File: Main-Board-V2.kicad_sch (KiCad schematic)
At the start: 12 parts, among them IC1 REG1117-5, J4 1-776163-5, U1 OPA325IDBVR, U2 Teensy4.0

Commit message: added LED indicators, fixed footprints
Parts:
- added D2, D3: LED, LED_SMD:LED_0805_2012Metric, symbol Device:LED
- added R29, R32: R_US, Resistor_SMD:R_0805_2012Metric, symbol Device:R_US
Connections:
- net +12V: now also R32.1
- net +5V: now also R29.1
- net GND: now also D2.1 (K), D3.1 (K)
- new net: D2.2 (A), R29.2
- new net: D3.2 (A), R32.2
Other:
- note added: "LED Power Indicators"
- note added: "Teensy 4.0 Pinout"
- title: (none) -> Main Board 2024
- moved on the sheet: C1, C2, C3, IC1, J4, R1, R2, R3, R4, R5, U1, U2

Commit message: idk, probably nothing
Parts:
- R29, R32: value R_US -> 150R
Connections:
- no-connect marks 34 -> 32
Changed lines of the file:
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@@
 	)
 	(no_connect
-		(at 236.22 106.68)
-	)
-	(no_connect
 		(at 292.1 99.06)
 	)
@@
 	)
 	(no_connect
-		(at 236.22 109.22)
-	)
-	(no_connect
 		(at 66.04 55.88)
 	)
@@
 			)
 		)
-		(property "Value" "R_US"
+		(property "Value" "150R"
 			(at 205.74 208.2799 0)
 			(effects
@@
 			)
 		)
-		(property "Value" "R_US"
+		(property "Value" "150R"
 			(at 180.34 208.2799 0)
 			(effects

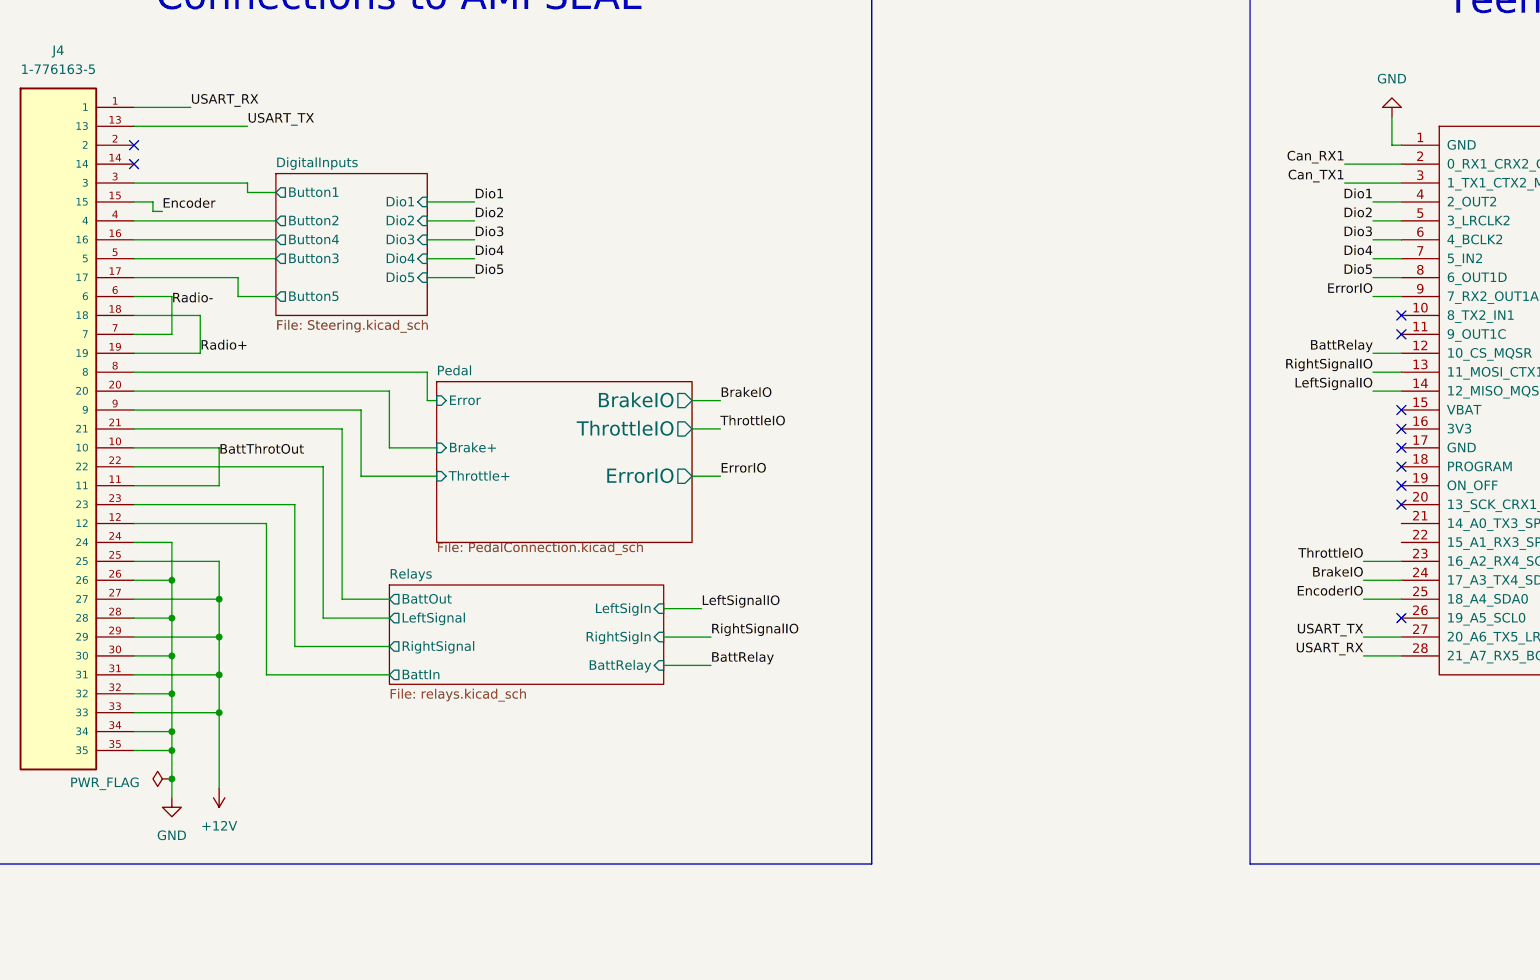
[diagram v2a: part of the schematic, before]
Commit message: redid 35 pos pinout
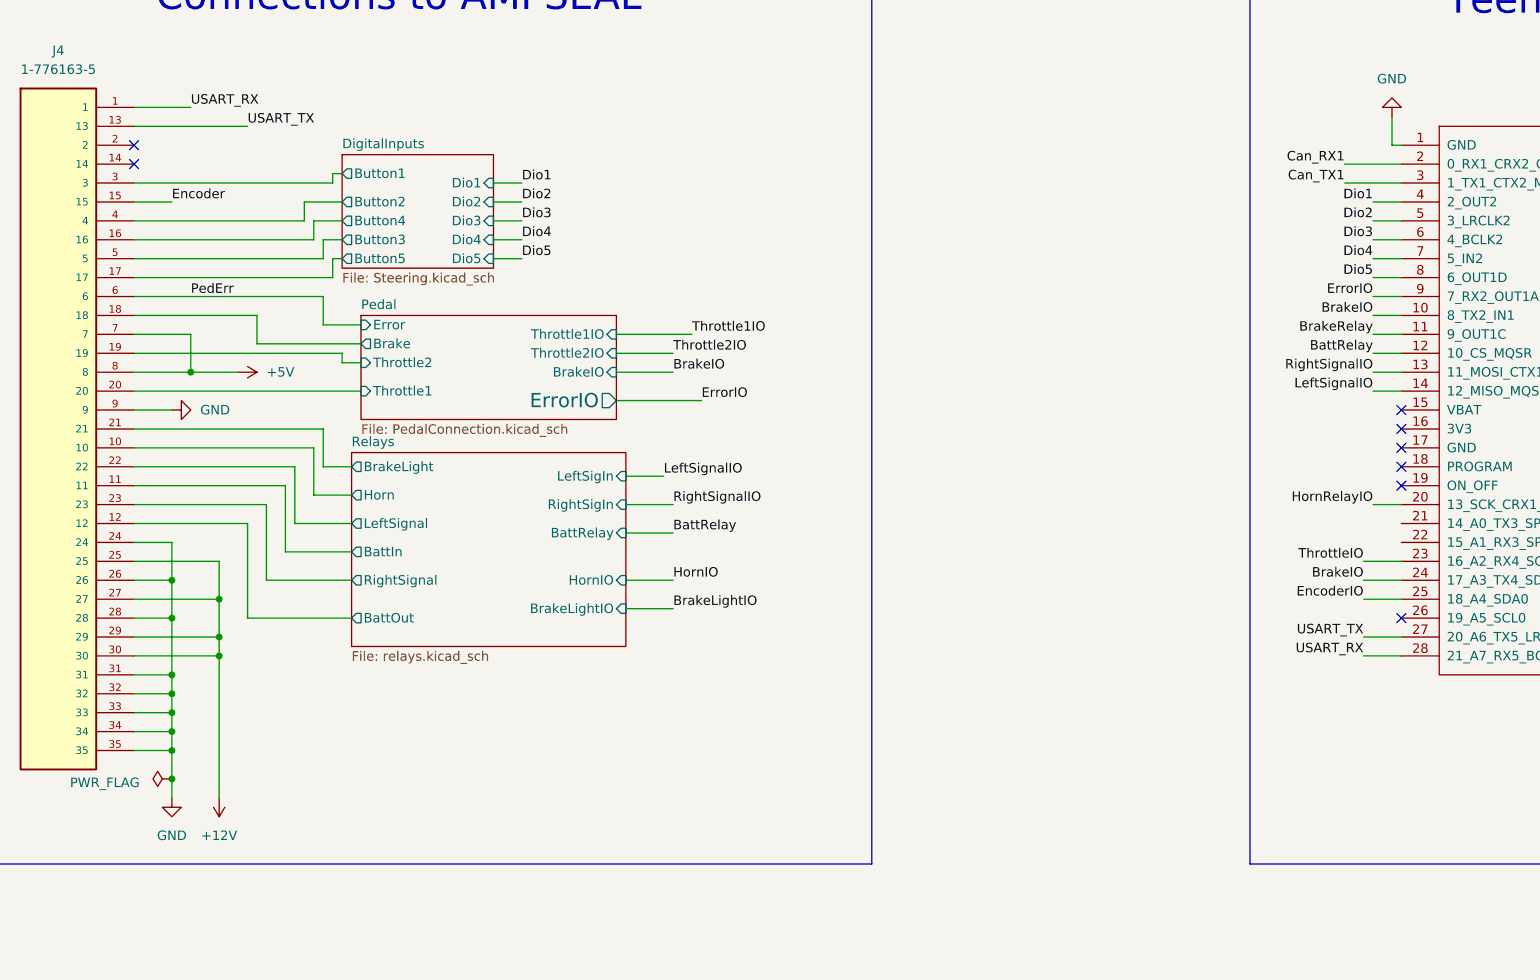
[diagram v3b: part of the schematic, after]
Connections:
- net Pedal/Error is gone; now on net +5V: J4.8
- net Pedal/Throttle+ is gone; now on net GND: J4.9
- net +12V: now also J4.30; no longer J4.31, J4.33
- net +5V: now also J4.7
- net BrakeIO: now also U2.10 (8_TX2_IN1)
- net GND: now also J4.31, J4.33; no longer J4.30
- net Relays/BattIn: now also J4.11; no longer J4.12
- net Relays/BattOut: now also J4.12; no longer J4.21
- net BrakeRelay: now reaches U2.11 (9_OUT1C)
- net HornRelayIO: now reaches U2.20 (13_SCK_CRX1_LED)
- net BattThrotOut renamed Relays/Horn
- net Relays/Horn: no longer J4.11
- net Pedal/Brake+ renamed Pedal/Throttle1
- net Radio+ renamed Pedal/Brake
- net Pedal/Brake: no longer J4.19
- net Radio- renamed PedErr
- net PedErr: no longer J4.7
- new net Pedal/Throttle2: J4.19
- new net Relays/BrakeLight: J4.21
- no-connect marks 32 -> 29
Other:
- sheet Pedal ports: added Brake, Throttle1, Throttle1IO, Throttle2, Throttle2IO; removed Brake+, Throttle+, ThrottleIO
- sheet Relays ports: added BrakeLight, BrakeLightIO, Horn, HornIO; removed none

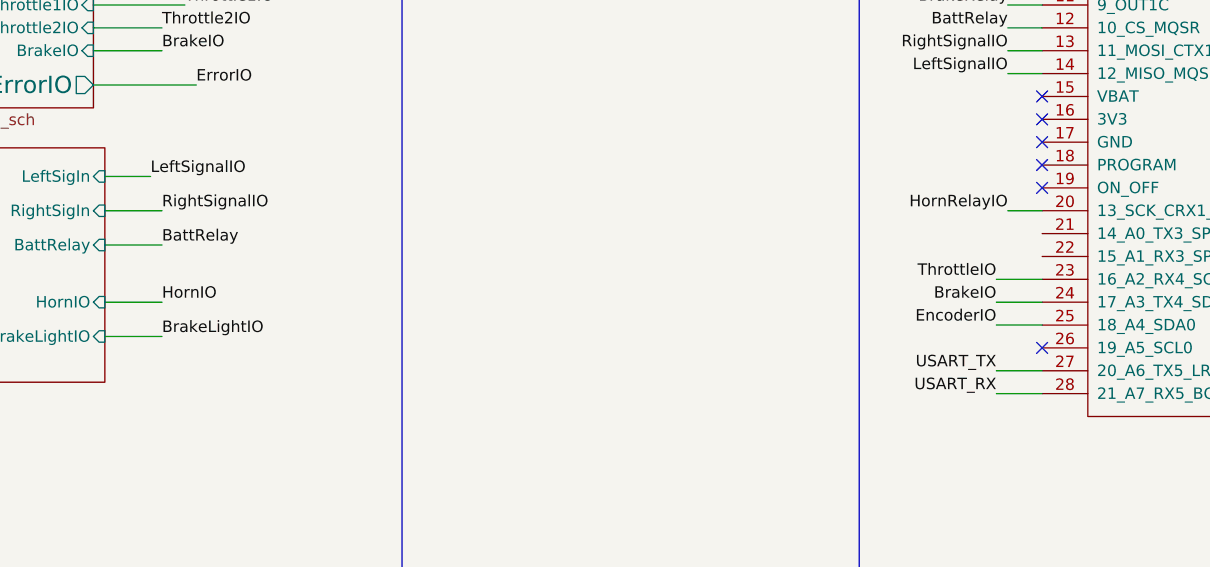
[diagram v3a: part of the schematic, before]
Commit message: fixed pcb excpet relays
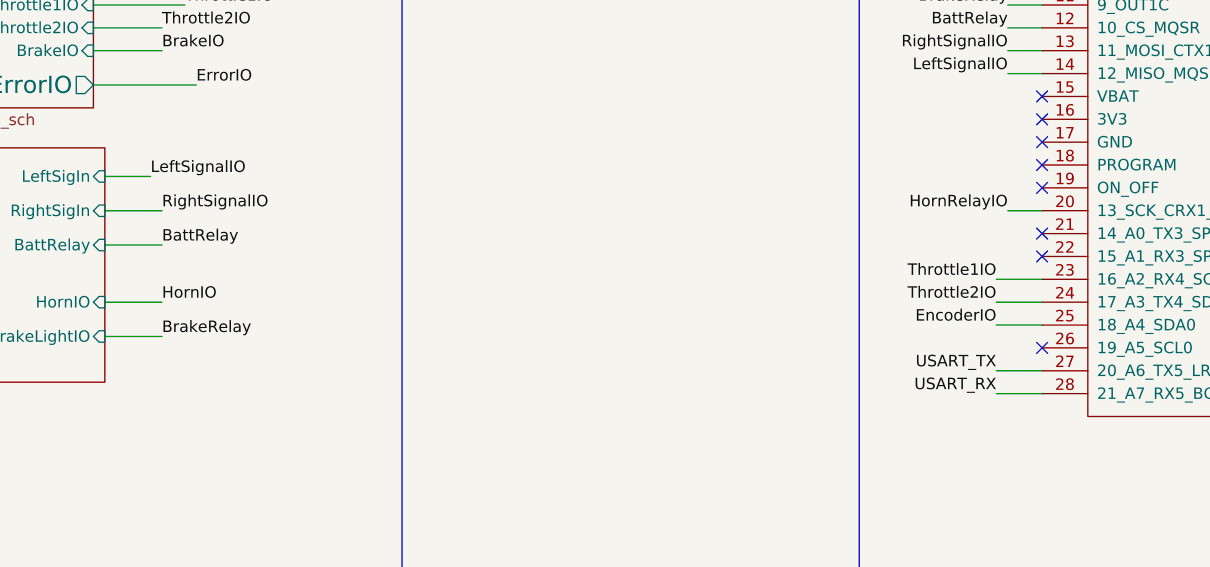
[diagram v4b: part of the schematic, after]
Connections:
- net ThrottleIO is gone; now on net Throttle1IO: U2.23 (16_A2_RX4_SCL1)
- net BrakeIO: no longer U2.24 (17_A3_TX4_SDA1)
- net Throttle2IO: now also U2.24 (17_A3_TX4_SDA1)
- no-connect marks 29 -> 31
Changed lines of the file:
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@@
+	)
+	(no_connect
+		(at 236.22 109.22)
 	)
 	(no_connect
@@
 	)
 	(no_connect
+		(at 236.22 106.68)
+	)
+	(no_connect
 		(at 292.1 86.36)
 	)
@@
 		)
 	)
-	(label "ThrottleIO"
+	(label "Throttle1IO"
 		(at 231.14 111.76 180)
 		(effects
@@
 		)
 	)
-	(label "BrakeIO"
+	(label "Throttle2IO"
 		(at 231.14 114.3 180)
 		(effects
@@
 		)
 	)
-	(label "BrakeLightIO"
+	(label "BrakeRelay"
 		(at 138.43 118.11 0)
 		(effects

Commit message: complete. Minor Tweaks
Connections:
- net HornRelayIO is gone; now on net BrakeRelay: U2.20 (13_SCK_CRX1_LED)
- net BrakeRelay: no longer U2.11 (9_OUT1C)
- net HornIO: now also U2.11 (9_OUT1C)
- net LeftSignalIO: now also U2.13 (11_MOSI_CTX1); no longer U2.14 (12_MISO_MQSL)
- net RightSignalIO: now also U2.14 (12_MISO_MQSL); no longer U2.13 (11_MOSI_CTX1)
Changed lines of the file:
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@@
+		)
+	)
+	(label "HornIO"
+		(at 232.41 81.28 180)
+		(effects
+			(font
+				(size 1.27 1.27)
+			)
+			(justify right bottom)
 		)
 	)
@@
 		)
 	)
+	(label "LeftSignalIO"
+		(at 232.41 86.36 180)
+		(effects
+			(font
+				(size 1.27 1.27)
+			)
+			(justify right bottom)
+		)
+	)
 	(label "ErrorIO"
 		(at 232.41 76.2 180)
@@
 		)
 	)
-	(label "LeftSignalIO"
-		(at 232.41 88.9 180)
-		(effects
-			(font
-				(size 1.27 1.27)
-			)
-			(justify right bottom)
-		)
-	)
 	(label "Encoder"
 		(at 273.05 212.09 180)
@@
 	)
 	(label "RightSignalIO"
-		(at 232.41 86.36 180)
+		(at 232.41 88.9 180)
 		(effects
 			(font
@@
 		)
 	)
-	(label "BrakeRelay"
-		(at 232.41 81.28 180)
-		(effects
-			(font
-				(size 1.27 1.27)
-			)
-			(justify right bottom)
-		)
-	)
 	(label "Dio3"
 		(at 232.41 68.58 180)
@@
 		)
 	)
+	(label "BrakeRelay"
+		(at 232.41 104.14 180)
+		(effects
+			(font
+				(size 1.27 1.27)
+			)
+			(justify right bottom)
+		)
+	)
 	(label "ErrorIO"
 		(at 142.24 90.17 0)
@@
 		(effects
 			(font
-				(size 1.27 1.27)
-			)
-			(justify right bottom)
-		)
-	)
-	(label "HornRelayIO"
-		(at 232.41 104.14 180)
-		(effects
-			(font

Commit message: removed resistors for light boards
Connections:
- net BrakeRelay: now also U2.13 (11_MOSI_CTX1); no longer U2.20 (13_SCK_CRX1_LED)
- net LeftSignalIO: now also U2.14 (12_MISO_MQSL); no longer U2.13 (11_MOSI_CTX1)
- net RightSignalIO: now also U2.20 (13_SCK_CRX1_LED); no longer U2.14 (12_MISO_MQSL)
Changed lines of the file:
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@@
+		)
+	)
+	(label "BrakeRelay"
+		(at 232.41 86.36 180)
+		(effects
+			(font
+				(size 1.27 1.27)
+			)
+			(justify right bottom)
 		)
 	)
@@
 		)
 	)
-	(label "LeftSignalIO"
-		(at 232.41 86.36 180)
-		(effects
-			(font
-				(size 1.27 1.27)
-			)
-			(justify right bottom)
-		)
-	)
 	(label "ErrorIO"
 		(at 232.41 76.2 180)
@@
 		)
 	)
-	(label "RightSignalIO"
-		(at 232.41 88.9 180)
-		(effects
-			(font
-				(size 1.27 1.27)
-			)
-			(justify right bottom)
-		)
-	)
 	(label "Dio5"
 		(at 118.11 71.12 0)
@@
 		)
 	)
+	(label "RightSignalIO"
+		(at 232.41 104.14 180)
+		(effects
+			(font
+				(size 1.27 1.27)
+			)
+			(justify right bottom)
+		)
+	)
 	(label "BrakeIO"
 		(at 138.43 86.36 0)
@@
 		)
 	)
-	(label "BrakeRelay"
-		(at 232.41 104.14 180)
-		(effects
-			(font
-				(size 1.27 1.27)
-			)
-			(justify right bottom)
-		)
-	)
 	(label "ErrorIO"
 		(at 142.24 90.17 0)
@@
 		)
 	)
+	(label "LeftSignalIO"
+		(at 232.41 88.9 180)
+		(effects
+			(font
+				(size 1.27 1.27)
+			)
+			(justify right bottom)
+		)
+	)

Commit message: front silkscreen
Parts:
- C1: value 1N -> 0.1U
- R3: value 10k -> 30k
- R5: value 1k -> 1000R
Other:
- note added: "12 V -> 3 V"
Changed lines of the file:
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@@
 		)
 	)
+	(text "12 V -> 3 V"
+		(exclude_from_sim no)
+		(at 295.91 201.93 0)
+		(effects
+			(font
+				(size 1.27 1.27)
+			)
+		)
+	)
 	(text "LED Power Indicators"
 		(exclude_from_sim no)
@@
 			)
 		)
-		(property "Value" "1N"
+		(property "Value" "0.1U"
 			(at 372.11 220.9799 0)
 			(show_name no)
@@
 			)
 		)
-		(property "Value" "1k"
+		(property "Value" "1000R"
 			(at 361.95 208.28 90)
 			(show_name no)
@@
 			)
 		)
-		(property "Value" "10k"
+		(property "Value" "30k"
 			(at 307.34 205.7399 0)
 			(show_name no)

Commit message: fixed relays
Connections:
- net BattRelay: now also U2.20 (13_SCK_CRX1_LED); no longer U2.12 (10_CS_MQSR)
- net BrakeRelay: now also U2.12 (10_CS_MQSR); no longer U2.13 (11_MOSI_CTX1)
- net LeftSignalIO: now also U2.13 (11_MOSI_CTX1); no longer U2.14 (12_MISO_MQSL)
- net RightSignalIO: now also U2.14 (12_MISO_MQSL); no longer U2.20 (13_SCK_CRX1_LED)
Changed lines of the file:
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@@
-		)
-	)
-	(label "BattRelay"
-		(at 232.41 83.82 180)
-		(effects
-			(font
-				(size 1.27 1.27)
-			)
-			(justify right bottom)
-		)
-	)
-	(label "BrakeRelay"
-		(at 232.41 86.36 180)
-		(effects
-			(font
-				(size 1.27 1.27)
-			)
-			(justify right bottom)
 		)
 	)
@@
 		)
 	)
+	(label "BrakeRelay"
+		(at 232.41 83.82 180)
+		(effects
+			(font
+				(size 1.27 1.27)
+			)
+			(justify right bottom)
+		)
+	)
 	(label "Throttle1IO"
 		(at 231.14 111.76 180)
@@
 		)
 	)
-	(label "RightSignalIO"
-		(at 232.41 104.14 180)
-		(effects
-			(font
-				(size 1.27 1.27)
-			)
-			(justify right bottom)
-		)
-	)
 	(label "BrakeIO"
 		(at 138.43 86.36 0)
@@
 		)
 	)
+	(label "RightSignalIO"
+		(at 232.41 88.9 180)
+		(effects
+			(font
+				(size 1.27 1.27)
+			)
+			(justify right bottom)
+		)
+	)
 	(label "Dio4"
 		(at 232.41 71.12 180)
@@
 		)
 	)
+	(label "LeftSignalIO"
+		(at 232.41 86.36 180)
+		(effects
+			(font
+				(size 1.27 1.27)
+			)
+			(justify right bottom)
+		)
+	)
 	(label "Dio3"
 		(at 118.11 66.04 0)
@@
 		)
 	)
+	(label "BattRelay"
+		(at 232.41 104.14 180)
+		(effects
+			(font
+				(size 1.27 1.27)
+			)
+			(justify right bottom)
+		)
+	)
 	(label "Throttle2IO"
 		(at 231.14 114.3 180)
@@
 		)
 	)
-	(label "LeftSignalIO"
-		(at 232.41 88.9 180)
-		(effects
-			(font
-				(size 1.27 1.27)
-			)
-			(justify right bottom)
-		)
-	)
